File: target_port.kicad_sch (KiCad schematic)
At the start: 32 parts, among them IC1 ECP5-BGA256, U13 DPO2036, U2 FUSB302B, U9 USB3343-CP

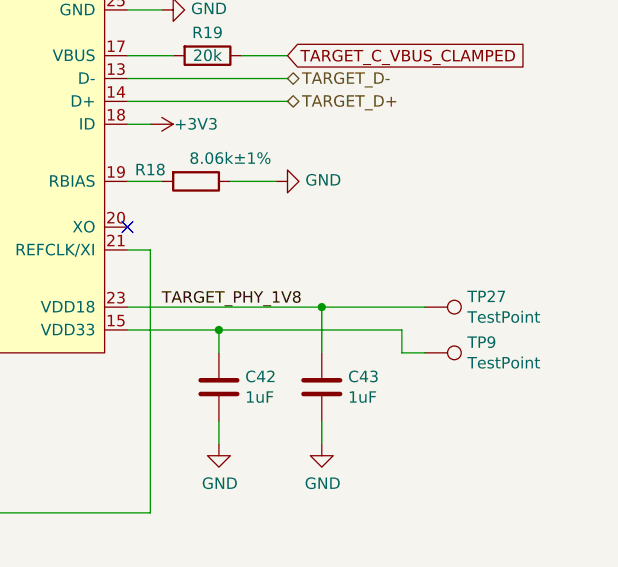
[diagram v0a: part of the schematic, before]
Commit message: Connect PHY pin 15 VDD33 to +3V3
This bypasses the PHY's internal 3.3 V regulator and ties it to the
board's +3V3 net, taking advantage of the superior decoupling of +3V3.
VDD33 test points are retained for test jig compatibility and in case
this change is reverted, but they could be removed in the future.
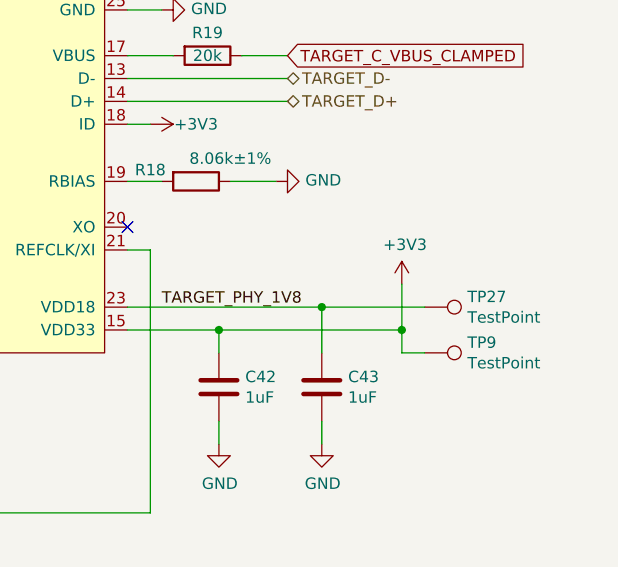
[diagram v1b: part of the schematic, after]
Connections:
- net +3V3: now also C42.1, TP9.1, U9.15 (VDD33)
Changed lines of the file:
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@@
   (junction (at 259.715 33.655) (diameter 0) (color 0 0 0 0)
+  )
+  (junction (at 256.54 135.89) (diameter 0) (color 0 0 0 0)
   )
   (junction (at 236.855 33.655) (diameter 0) (color 0 0 0 0)
@@
   )
   (wire (pts (xy 248.285 33.655) (xy 236.855 33.655))
+    (stroke (width 0) (type default) (color 0 0 0 0))
+  )
+  (wire (pts (xy 256.54 130.81) (xy 256.54 135.89))
     (stroke (width 0) (type default) (color 0 0 0 0))
   )
@@
     (pin "9")
   )
+  (symbol (lib_id "power:+3V3") (at 256.54 130.81 0) (unit 1)
+    (in_bom yes) (on_board yes)
+    (property "Reference" "#PWR071" (id 0) (at 256.54 134.62 0)
+      (effects (font (size 1.27 1.27)) hide)
+    )
+    (property "Value" "+3V3" (id 1) (at 256.8956 126.4158 0))
+    (property "Footprint" "" (id 2) (at 256.54 130.81 0)
+      (effects (font (size 1.27 1.27)) hide)
+    )
+    (property "Datasheet" "" (id 3) (at 256.54 130.81 0)
+      (effects (font (size 1.27 1.27)) hide)
+    )
+    (pin "1")
+  )
   (symbol (lib_id "power:+3V3") (at 120.65 32.385 0) (unit 1)

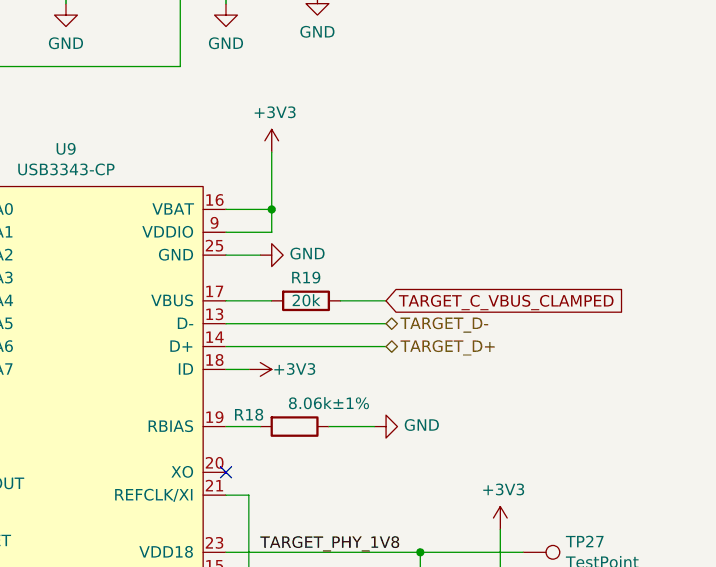
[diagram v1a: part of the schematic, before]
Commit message: Add a common-mode choke to each USB PHY
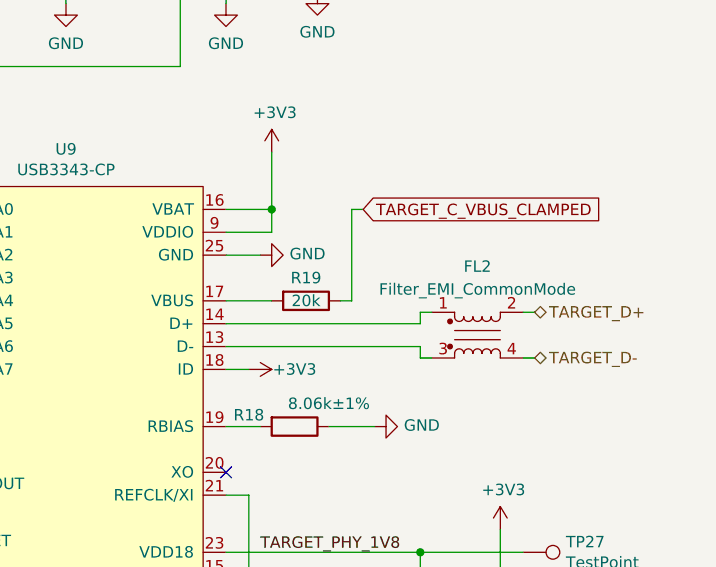
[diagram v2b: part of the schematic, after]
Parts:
- added FL2: Filter_EMI_CommonMode, cynthion:L_CommonModeChoke_Murata_DLM0NS, symbol Device:Filter_EMI_CommonMode
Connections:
- net TARGET_D+: now also FL2.2; no longer U9.14 (D+)
- net TARGET_D-: now also FL2.4; no longer U9.13 (D-)
- new net: FL2.3, U9.13 (D-)
- new net: FL2.1, U9.14 (D+)
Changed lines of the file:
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@@
+    (stroke (width 0) (type default) (color 0 0 0 0))
+  )
+  (wire (pts (xy 247.65 107.95) (xy 247.65 106.68))
     (stroke (width 0) (type default) (color 0 0 0 0))
   )
@@
     (stroke (width 0) (type default) (color 0 0 0 0))
   )
-  (wire (pts (xy 238.76 105.41) (xy 243.84 105.41))
-    (stroke (width 0) (type default) (color 0 0 0 0))
-  )
   (wire (pts (xy 116.84 132.08) (xy 116.84 124.46))
     (stroke (width 0) (type default) (color 0 0 0 0))
@@
     (stroke (width 0) (type default) (color 0 0 0 0))
   )
+  (wire (pts (xy 259.08 106.68) (xy 260.35 106.68))
+    (stroke (width 0) (type default) (color 0 0 0 0))
+  )
   (wire (pts (xy 226.06 71.12) (xy 226.06 72.39))
     (stroke (width 0) (type default) (color 0 0 0 0))
@@
     (stroke (width 0) (type default) (color 0 0 0 0))
   )
+  (wire (pts (xy 260.35 111.76) (xy 259.08 111.76))
+    (stroke (width 0) (type default) (color 0 0 0 0))
+  )
   (wire (pts (xy 208.28 71.12) (xy 208.28 69.85))
     (stroke (width 0) (type default) (color 0 0 0 0))
@@
     (stroke (width 0) (type default) (color 0 0 0 0))
   )
+  (wire (pts (xy 247.65 111.76) (xy 248.92 111.76))
+    (stroke (width 0) (type default) (color 0 0 0 0))
+  )
   (wire (pts (xy 118.11 113.03) (xy 118.11 100.33))
     (stroke (width 0) (type default) (color 0 0 0 0))
@@
     (stroke (width 0) (type default) (color 0 0 0 0))
   )
+  (wire (pts (xy 240.03 105.41) (xy 240.03 95.25))
+    (stroke (width 0) (type default) (color 0 0 0 0))
+  )
   (wire (pts (xy 159.385 47.625) (xy 159.385 48.895))
     (stroke (width 0) (type default) (color 0 0 0 0))
@@
     (stroke (width 0) (type default) (color 0 0 0 0))
   )
-  (wire (pts (xy 226.06 110.49) (xy 243.84 110.49))
+  (wire (pts (xy 226.06 110.49) (xy 247.65 110.49))
     (stroke (width 0) (type default) (color 0 0 0 0))
   )
@@
     (stroke (width 0) (type default) (color 0 0 0 0))
   )
-  (wire (pts (xy 226.06 107.95) (xy 243.84 107.95))
+  (wire (pts (xy 226.06 107.95) (xy 247.65 107.95))
     (stroke (width 0) (type default) (color 0 0 0 0))
   )
@@
     (stroke (width 0) (type default) (color 0 0 0 0))
   )
+  (wire (pts (xy 240.03 95.25) (xy 241.3 95.25))
+    (stroke (width 0) (type default) (color 0 0 0 0))
+  )
   (wire (pts (xy 259.715 32.385) (xy 259.715 33.655))
     (stroke (width 0) (type default) (color 0 0 0 0))
@@
     (stroke (width 0) (type default) (color 0 0 0 0))
   )
+  (wire (pts (xy 238.76 105.41) (xy 240.03 105.41))
+    (stroke (width 0) (type default) (color 0 0 0 0))
+  )
   (bus (pts (xy 139.7 166.37) (xy 139.7 168.91))
     (stroke (width 0) (type default) (color 0 0 0 0))
@@
     (stroke (width 0) (type default) (color 0 0 0 0))
   )
+  (wire (pts (xy 247.65 110.49) (xy 247.65 111.76))
+    (stroke (width 0) (type default) (color 0 0 0 0))
+  )
   (wire (pts (xy 50.8 74.93) (xy 73.66 74.93))
     (stroke (width 0) (type default) (color 0 0 0 0))
@@
     (stroke (width 0) (type default) (color 0 0 0 0))
   )
+  (wire (pts (xy 247.65 106.68) (xy 248.92 106.68))
+    (stroke (width 0) (type default) (color 0 0 0 0))
+  )
   (wire (pts (xy 148.59 59.69) (xy 114.3 59.69))
     (stroke (width 0) (type default) (color 0 0 0 0))
@@
     (effects (font (size 1.27 1.27)) (justify left bottom))
   )
-  (global_label "TARGET_C_VBUS_CLAMPED" (shape input) (at 243.84 105.41 0) (fields_autoplaced)
+  (global_label "TARGET_C_VBUS_CLAMPED" (shape input) (at 241.3 95.25 0) (fields_autoplaced)
     (effects (font (size 1.27 1.27)) (justify left))
-    (property "Intersheet References" "${INTERSHEET_REFS}" (id 0) (at 270.4756 105.3306 0)
+    (property "Intersheet References" "${INTERSHEET_REFS}" (id 0) (at 267.9356 95.1706 0)
       (effects (font (size 1.27 1.27)) (justify left) hide)
     )
@@
     (effects (font (size 1.27 1.27)) (justify left))
   )
-  (hierarchical_label "TARGET_D+" (shape bidirectional) (at 243.84 110.49 0)
+  (hierarchical_label "TARGET_D+" (shape bidirectional) (at 260.35 106.68 0)
     (effects (font (size 1.27 1.27)) (justify left))
   )
@@
     (effects (font (size 1.27 1.27)) (justify left))
   )
-  (hierarchical_label "TARGET_D-" (shape bidirectional) (at 243.84 107.95 0)
+  (hierarchical_label "TARGET_D-" (shape bidirectional) (at 260.35 111.76 0)
     (effects (font (size 1.27 1.27)) (justify left))
   )
@@
     (pin "2")
   )
+  (symbol (lib_id "Device:Filter_EMI_CommonMode") (at 254 109.22 0) (unit 1)
+    (in_bom yes) (on_board yes)
+    (property "Reference" "FL2" (id 0) (at 254 101.6 0))
+    (property "Value" "Filter_EMI_CommonMode" (id 1) (at 254 104.1369 0))
+    (property "Footprint" "cynthion:L_CommonModeChoke_Murata_DLM0NS" (id 2) (at 254 108.204 0)
+      (effects (font (size 1.27 1.27)) hide)
+    )
+    (property "Datasheet" "https://www.murata.com/en-global/products/productdata/8799424610334/EFLD0009.pdf" (id 3) (at 254 108.204 0)
+      (effects (font (size 1.27 1.27)) hide)
+    )
+    (property "Description" "CMC 100MA 2LN 90 OHM SMD" (id 4) (at 254 109.22 0)
+      (effects (font (size 1.27 1.27)) hide)
+    )
+    (property "Manufacturer" "Murata" (id 5) (at 254 109.22 0)
+      (effects (font (size 1.27 1.27)) hide)
+    )
+    (property "Part Number" "DLM0NSN900HY2D" (id 6) (at 254 109.22 0)
+      (effects (font (size 1.27 1.27)) hide)
+    )
+    (pin "1")
+    (pin "2")
+    (pin "3")
+    (pin "4")
+  )
   (symbol (lib_id "power:GND") (at 120.65 52.705 0) (mirror y) (unit 1)

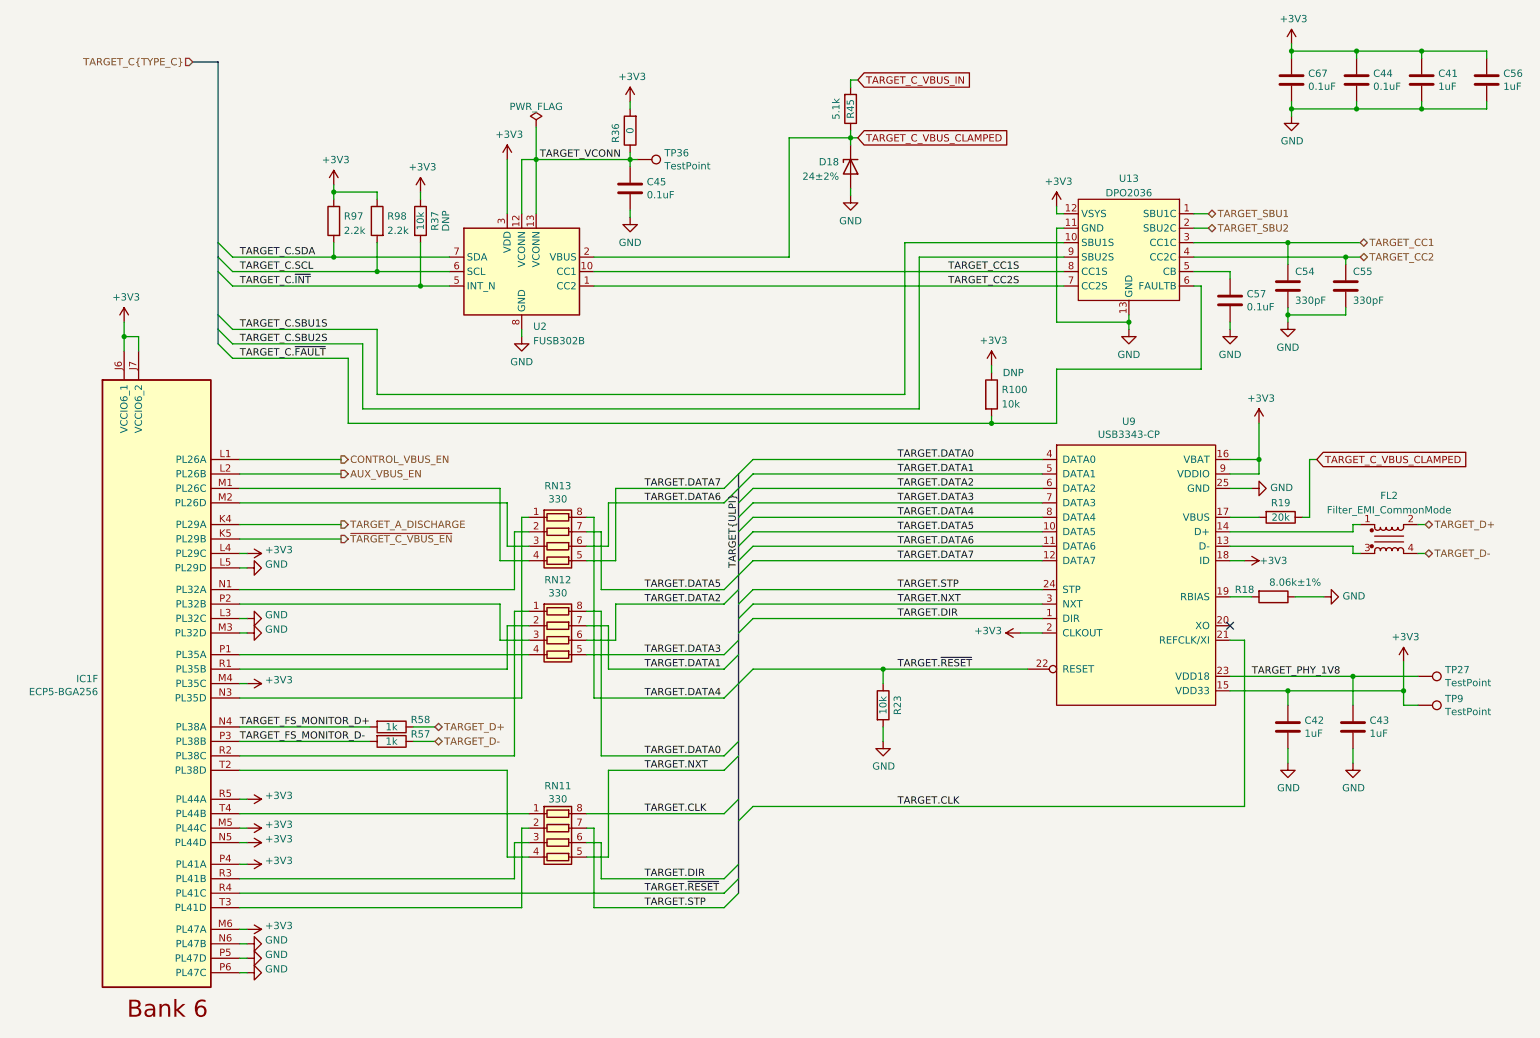
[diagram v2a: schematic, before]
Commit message: Rearrange schematic for readability
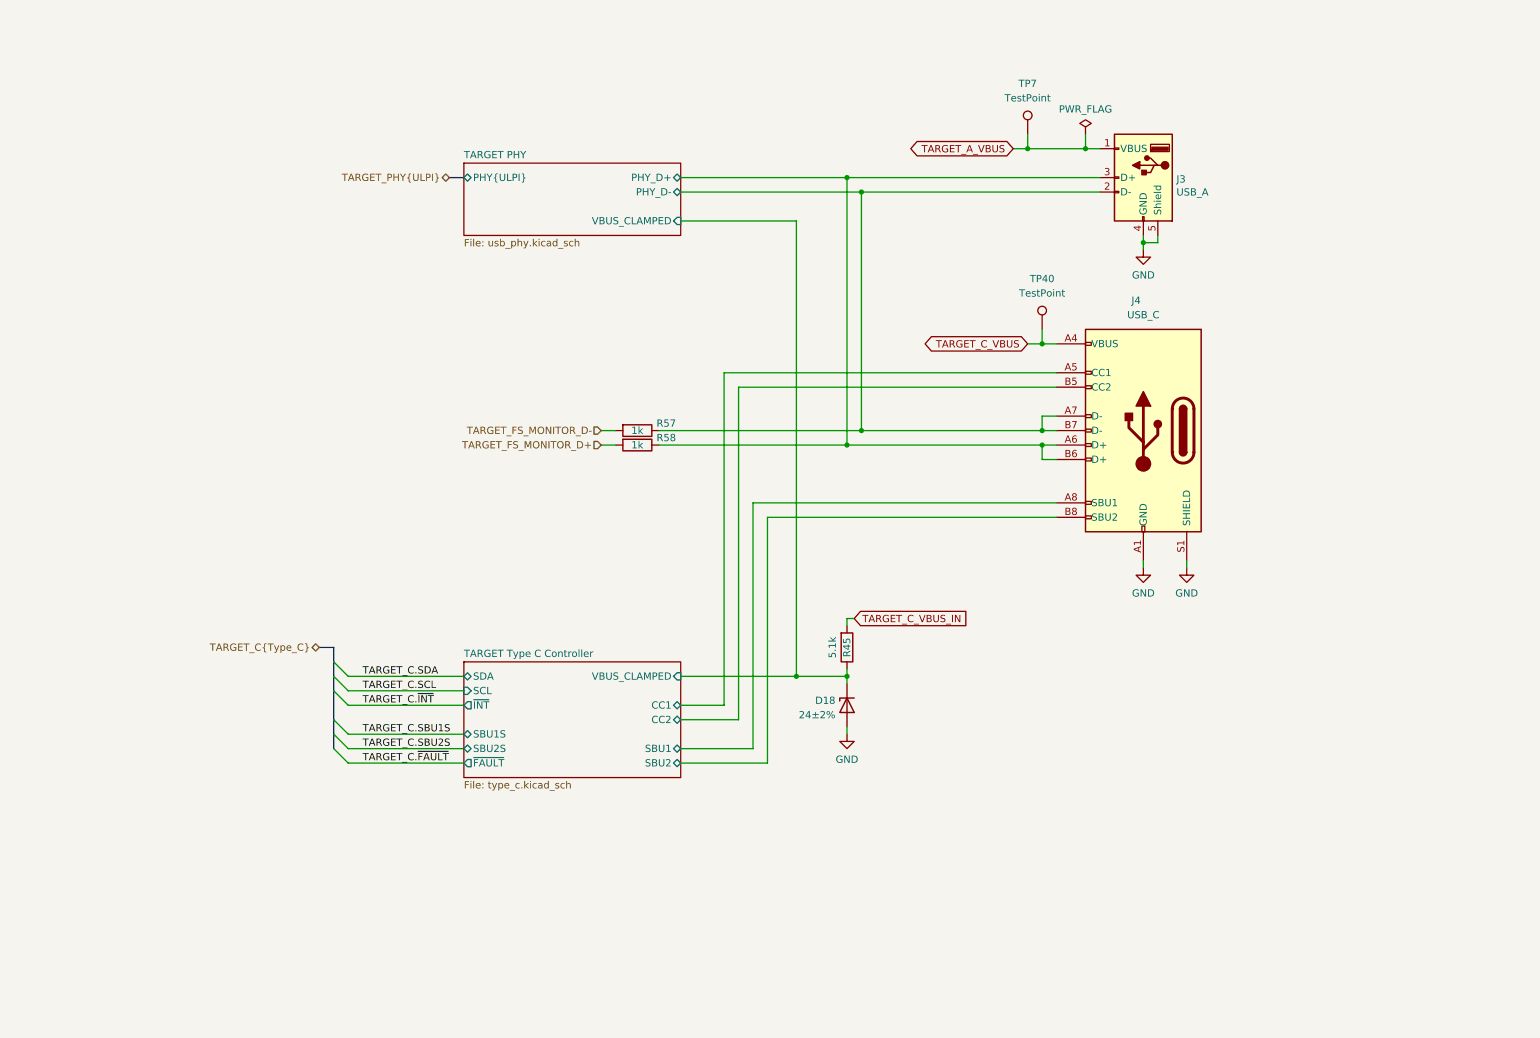
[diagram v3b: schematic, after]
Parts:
- removed C41, C42, C43, C56: 1uF, Capacitor_SMD:C_0402_1005Metric, symbol Device:C
- removed C44, C45, C57, C67: 0.1uF, Capacitor_SMD:C_0402_1005Metric, symbol Device:C
- removed C54, C55: 330pF, Capacitor_SMD:C_0402_1005Metric, symbol Device:C
- removed FL2: Filter_EMI_CommonMode, cynthion:L_CommonModeChoke_Murata_DLM0NS, symbol Device:Filter_EMI_CommonMode
- removed IC1: ECP5-BGA256, cynthion:lattice_cabga256, symbol fpgas_and_processors:ECP5-BGA256
- removed R100, R23, R37: 10k, Resistor_SMD:R_0402_1005Metric, symbol Device:R
- removed R18: 8.06k±1%, Resistor_SMD:R_0402_1005Metric, symbol Device:R
- removed R19: 20k, Resistor_SMD:R_0402_1005Metric, symbol Device:R
- removed R36: 0, Resistor_SMD:R_0402_1005Metric, symbol Device:R
- removed R97, R98: 2.2k, Resistor_SMD:R_0402_1005Metric, symbol Device:R
- removed RN11, RN12, RN13: 330, Resistor_SMD:R_Array_Convex_4x0402, symbol Device:R_Pack04
- removed TP27, TP36, TP9: TestPoint, TestPoint:TestPoint_Pad_D1.0mm, symbol Connector:TestPoint
- removed U13: DPO2036, cynthion:Diodes_UQFN2020-12_Type-B, symbol usb:DPO2036
- removed U2: FUSB302B, Package_DFN_QFN:WQFN-14-1EP_2.5x2.5mm_P0.5mm_EP1.45x1.45mm, symbol Interface_USB:FUSB302BMPX
- removed U9: USB3343-CP, Package_DFN_QFN:VQFN-24-1EP_4x4mm_P0.5mm_EP2.45x2.45mm, symbol usb:USB3343
- added J3: USB_A, cynthion:USB_A_Kycon_KUSBXHT-SB-AS1N-B30-NF_Horizontal, symbol Connector:USB_A
- added J4: USB_C, cynthion:USB_C_Receptacle_HRO_TYPE-C-31-M-12, symbol Connector:USB_C_Receptacle_USB2.0
- added TP40, TP7: TestPoint, TestPoint:TestPoint_Pad_D1.0mm, symbol Connector:TestPoint
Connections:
- net GND: now also J3.4 (GND), J3.5 (Shield), J4.A1 (GND), J4.A12 (GND), J4.B1 (GND), J4.B12 (GND), J4.S1 (SHIELD)
- net TARGET_C_VBUS_CLAMPED renamed TARGET PHY/VBUS_CLAMPED
- net TARGET_D+ renamed TARGET PHY/PHY_D+
- net TARGET PHY/PHY_D+: now also J3.3 (D+), J4.A6 (D+), J4.B6 (D+)
- net TARGET_D- renamed TARGET PHY/PHY_D-
- net TARGET PHY/PHY_D-: now also J3.2 (D-), J4.A7 (D-), J4.B7 (D-)
- new net TARGET Type C Controller/CC1: J4.A5 (CC1)
- new net TARGET Type C Controller/CC2: J4.B5 (CC2)
- new net TARGET Type C Controller/SBU1: J4.A8 (SBU1)
- new net TARGET Type C Controller/SBU2: J4.B8 (SBU2)
- new net TARGET_A_VBUS: J3.1 (VBUS), TP7.1
- new net TARGET_C_VBUS: J4.A4 (VBUS), J4.A9 (VBUS), J4.B4 (VBUS), J4.B9 (VBUS), TP40.1
- no-connect marks 1 -> 0
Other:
- added sheet TARGET PHY (usb_phy.kicad_sch)
- added sheet TARGET Type C Controller (type_c.kicad_sch)
- moved on the sheet: D18, R45, R57, R58

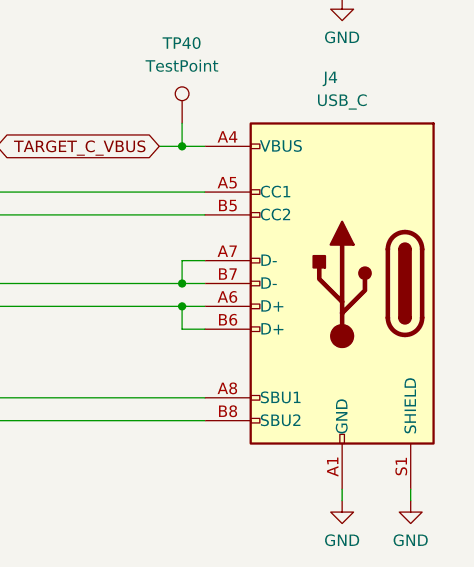
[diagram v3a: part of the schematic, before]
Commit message: Upgrade to KiCad 7
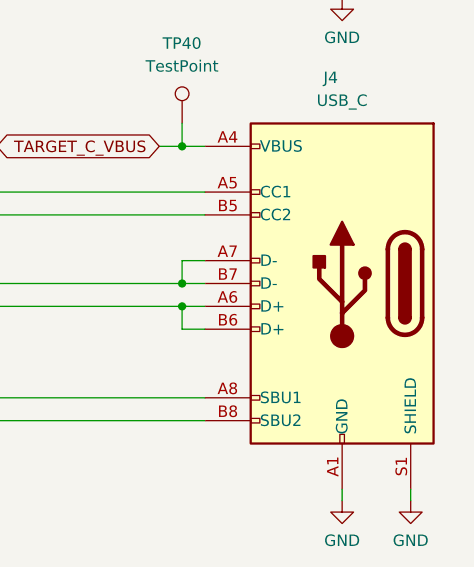
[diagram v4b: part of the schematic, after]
